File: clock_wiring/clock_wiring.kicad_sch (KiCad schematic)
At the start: 18 parts

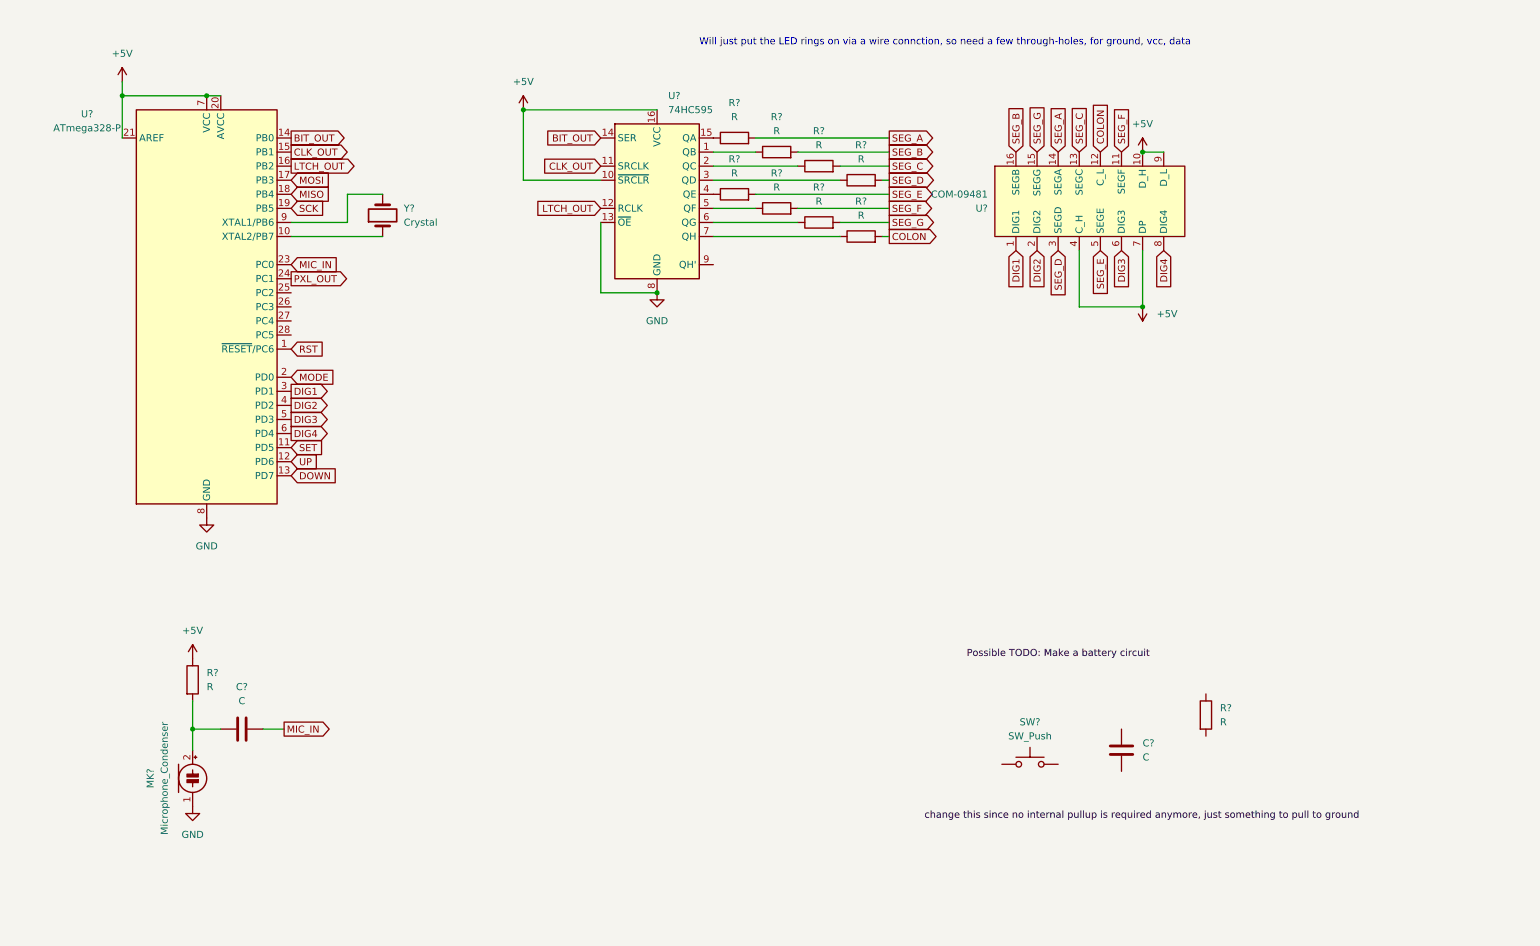
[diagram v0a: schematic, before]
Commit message: updates to 7seg writing, added buttons to schematic (researching mic output voltages)
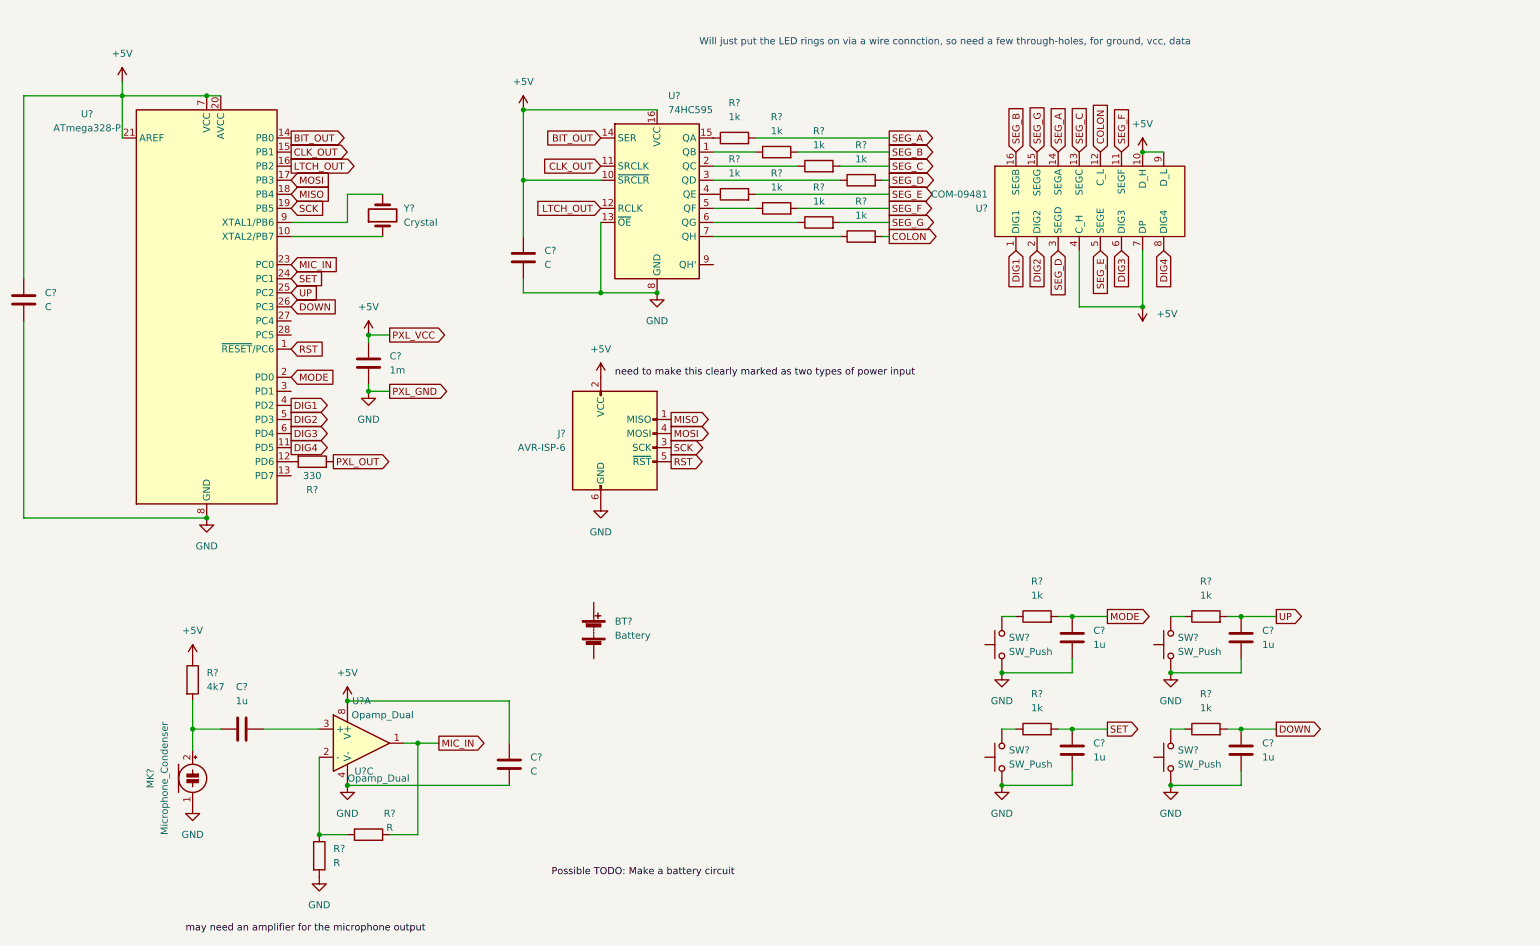
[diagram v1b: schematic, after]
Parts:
- added BT?: Battery, symbol Device:Battery
- added C? (x3): 1u, symbol Device:C
- added C? (x3): C, symbol Device:C
- added C?: 1m, symbol Device:C
- added J?: AVR-ISP-6, symbol Connector:AVR-ISP-6
- added R? (x3): 1k, symbol Device:R
- added R? (x2): R, symbol Device:R
- added R?: 330, symbol Device:R
- added SW? (x3): SW_Push, symbol Switch:SW_Push
- added U? (x2): Opamp_Dual, symbol Device:Opamp_Dual
- C? (x2): value C -> 1u
- R? (x9): value R -> 1k
- R?: value R -> 4k7
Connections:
- net +5V: now also C?.1, C?.1, C?.1, C?.2, J?.2 (VCC), U?.8 (V+)
- net DIG1: now also U?.4 (PD2); no longer U?.3 (PD1)
- net DIG2: now also U?.5 (PD3); no longer U?.4 (PD2)
- net DIG3: now also U?.6 (PD4); no longer U?.5 (PD3)
- net DIG4: now also U?.11 (PD5); no longer U?.6 (PD4)
- net DOWN: now also U?.26 (PC3), C?.1, R?.2; no longer U?.13 (PD7)
- net GND: now also C?.2, SW?.1, C?.1, C?.2, C?.2, C?.2, C?.2, C?.2, C?.2, J?.6 (GND), R?.2, SW?.1, SW?.1, SW?.1, U?.4 (V-)
- net MIC_IN: now also R?.2, U?.1; no longer C?.2
- net MISO: now also J?.1 (MISO)
- net MODE: now also C?.1, R?.2
- net MOSI: now also J?.4 (MOSI)
- net PXL_OUT: now also R?.1; no longer U?.24 (PC1)
- net RST: now also J?.5 (~{RST})
- net SCK: now also J?.3 (SCK)
- net SET: now also U?.24 (PC1), C?.1, R?.2; no longer U?.11 (PD5)
- net UP: now also U?.25 (PC2), C?.1, R?.2; no longer U?.12 (PD6)
- net at R?.1: now also SW?.2
- new net: R?.1, SW?.2 (x3)
- new net: R?.1, R?.1, U?.2 (-)
- new net: C?.2, U?.3 (+)
- new net: R?.2, U?.12 (PD6)
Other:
- moved on the sheet: C?, R?, SW?

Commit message: switched to rtc usage rather than internal clock, partial mode button changes, schematic updates and mic removal
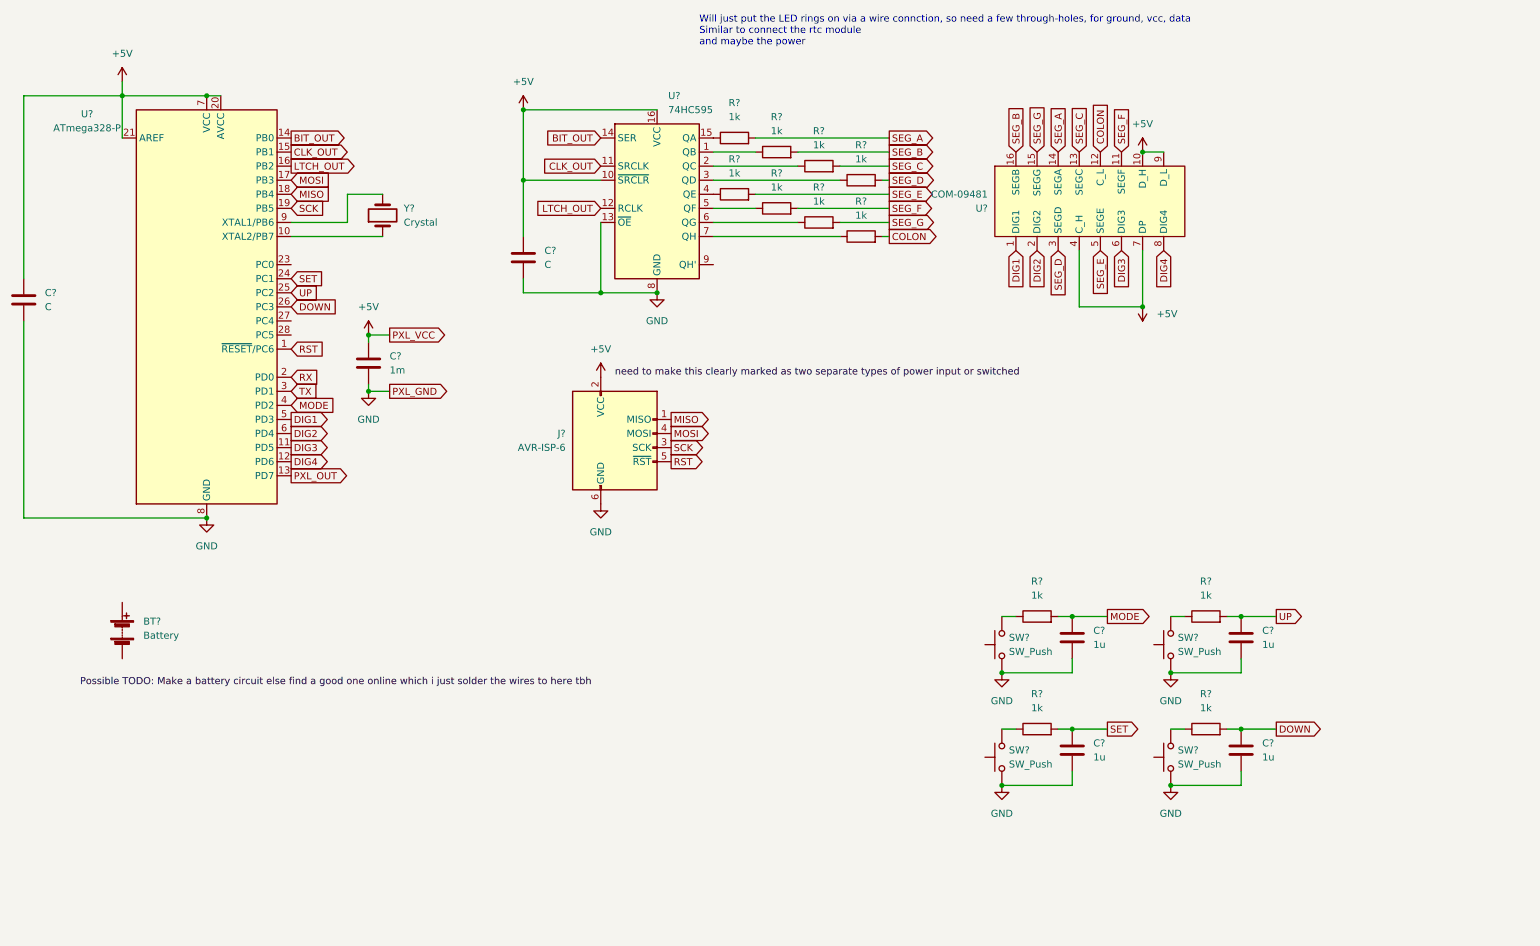
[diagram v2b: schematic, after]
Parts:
- removed C?: C, symbol Device:C
- removed C?: 1u, symbol Device:C
- removed MK?: Microphone_Condenser, symbol Device:Microphone_Condenser
- removed R?: 4k7, symbol Device:R
- removed R? (x2): R, symbol Device:R
- removed R?: 330, symbol Device:R
- removed U? (x2): Opamp_Dual, symbol Device:Opamp_Dual
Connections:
- net DIG1: now also U?.5 (PD3); no longer U?.4 (PD2)
- net DIG2: now also U?.6 (PD4); no longer U?.5 (PD3)
- net DIG3: now also U?.11 (PD5); no longer U?.6 (PD4)
- net DIG4: now also U?.12 (PD6); no longer U?.11 (PD5)
- net MODE: now also U?.4 (PD2); no longer U?.2 (PD0)
- net PXL_OUT: now also U?.13 (PD7)
- net TX: now reaches U?.3 (PD1)
- net MIC_IN: no longer names the net of U?.23 (PC0)
- new net RX: U?.2 (PD0)
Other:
- note added: "Will just put the LED rings on via a wire connction, so need a few through-holes, for ground, vcc, data Similar to connect the rtc module and maybe the power"
- note removed: "Will just put the LED rings on via a wire connction, so need a few through-holes, for ground, vcc, data"
- moved on the sheet: BT?

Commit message: some more pcb progress before adding layout + maybe power circuit change
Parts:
- removed BT?: Battery, symbol Device:Battery
- added C8, C9: 22p, Capacitor_SMD:C_1206_3216Metric_Pad1.33x1.80mm_HandSolder, symbol Device:C
- added J1, J2, J3, J4, J5, J6, J8: Conn_01x01_Female, Connector_Pin:Pin_D1.0mm_L10.0mm_LooseFit, symbol Connector:Conn_01x01_Female
- added U5: TinyRTC, clock:TinyRTC, symbol clock_libs:TinyRTC
- C1, C2, C3, C4, C5: renamed from C?; footprint (none) -> Capacitor_SMD:C_1206_3216Metric_Pad1.33x1.80mm_HandSolder
- C6, C7: renamed from C?; value C -> 1m; footprint (none) -> Capacitor_SMD:C_1206_3216Metric_Pad1.33x1.80mm_HandSolder
- R1, R10, R11, R12, R2, R3, R4, R5, R6, R7, R8, R9: renamed from R?; footprint (none) -> Resistor_SMD:R_1206_3216Metric_Pad1.30x1.75mm_HandSolder
- SW1, SW2, SW3, SW4: renamed from SW?; footprint (none) -> Button_Switch_THT:SW_Tactile_Straight_KSA0Axx1LFTR
- U1: renamed from U?; footprint Package_DIP:DIP-28_W7.62mm -> Package_DIP:DIP-28_W7.62mm_Socket
- U2: renamed from U?; footprint (none) -> Package_DIP:DIP-16_W7.62mm
- U3: renamed from U?; footprint (none) -> clock:COM-09481
- U4: renamed from J?; footprint (none) -> Connector_PinHeader_2.00mm:PinHeader_2x03_P2.00mm_Vertical
- Y1: renamed from Y?; footprint (none) -> Crystal:Crystal_HC52-6mm_Vertical
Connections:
- net +5V: now also J1.1 (Pin_1), J3.1 (Pin_1), U5.3 (VCC)
- net GND: now also J2.1 (Pin_1), J4.1 (Pin_1), U5.2 (GND)
- net PXL_OUT: now also J5.1 (Pin_1)
- net RX: now also J6.1 (Pin_1)
- net TX: now also J8.1 (Pin_1)
- net at U1.10 (XTAL2/PB7), Y1.1: now also C8.2
- net SDA: now reaches U1.27 (PC4)
- net SDA: now also U5.4 (SDA)
- net SCL: now reaches U1.28 (PC5)
- net SCL: now also U5.5 (SCL)
- net at U1.9 (XTAL1/PB6), Y1.2: now also C9.1
- new net: C8.1, C9.2
- no-connect marks 0 -> 5
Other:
- note removed: "Will just put the LED rings on via a wire connction, so need a few through-holes, for ground, vcc, data Similar to connect the rtc module and maybe the power"
- moved on the sheet: C1, C2, C3, C4, C5, R1, R2, R3, R4, SW1, SW2, SW3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
